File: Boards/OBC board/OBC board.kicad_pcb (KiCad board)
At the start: 4 copper layers, 75 x 48 mm, 92 parts, among them J1 BM03B-SRSS-TBLFSN, J2 USB_C, J3 Conn_01x01_Socket, J4 Conn_01x04_Socket, J5 Conn_01x04_Socket, J6 XT30UPB-M, J7 Conn_01x01_Socket, SW1 SW_Push, SW2 SW_Push, SW3 D2F-01-D, U1 ESD7L5.0DT5G, U10 IRLZ44NPBF, U2 ST1L05APU33R, U3 MAX485CSA+T, U4 ASM330LHH, U5 TPS1120DR, U6 TPS1120DR, U7 TPS1120DR, U8 LPS22DFTR, U9 LIS2MDLTR

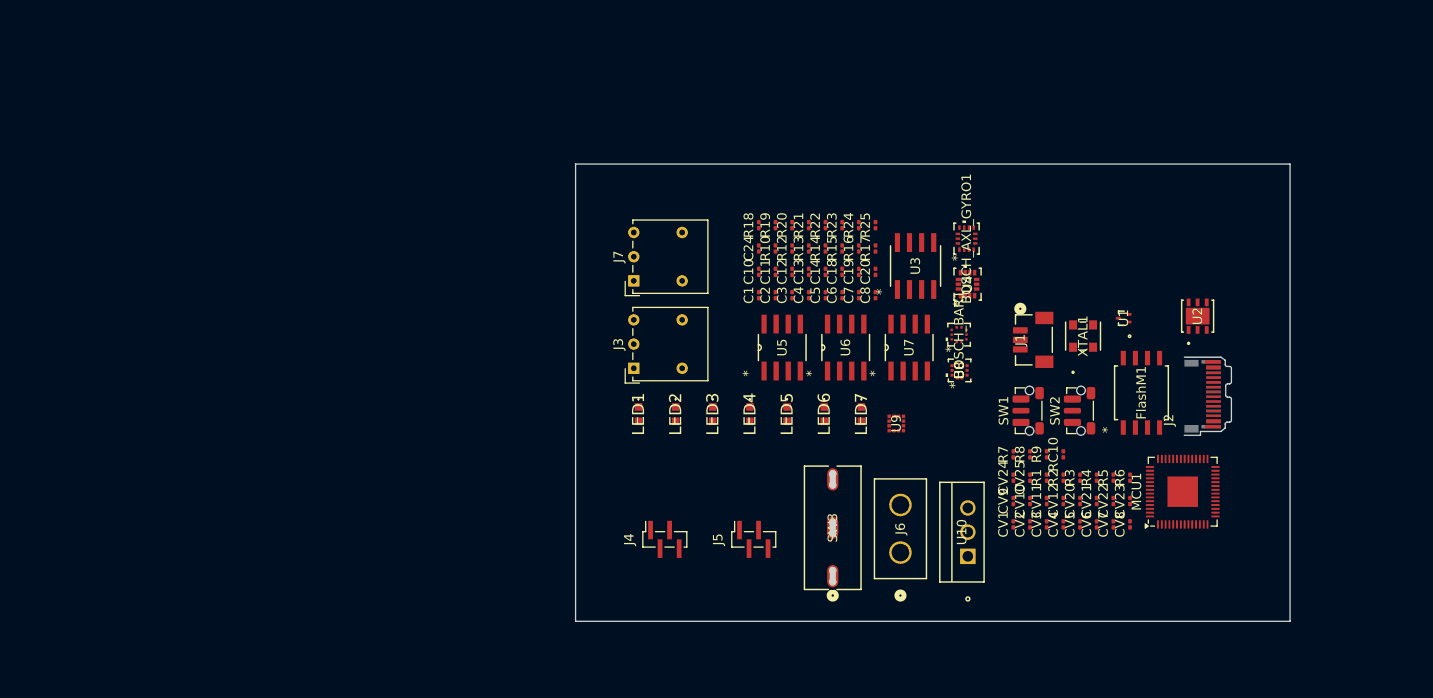
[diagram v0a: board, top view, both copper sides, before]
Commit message: Adição de Connectors
Connector "CONN Female Header 22022065" adicionado à library
Connectors do UART, 5V e GND adicionados à OBC
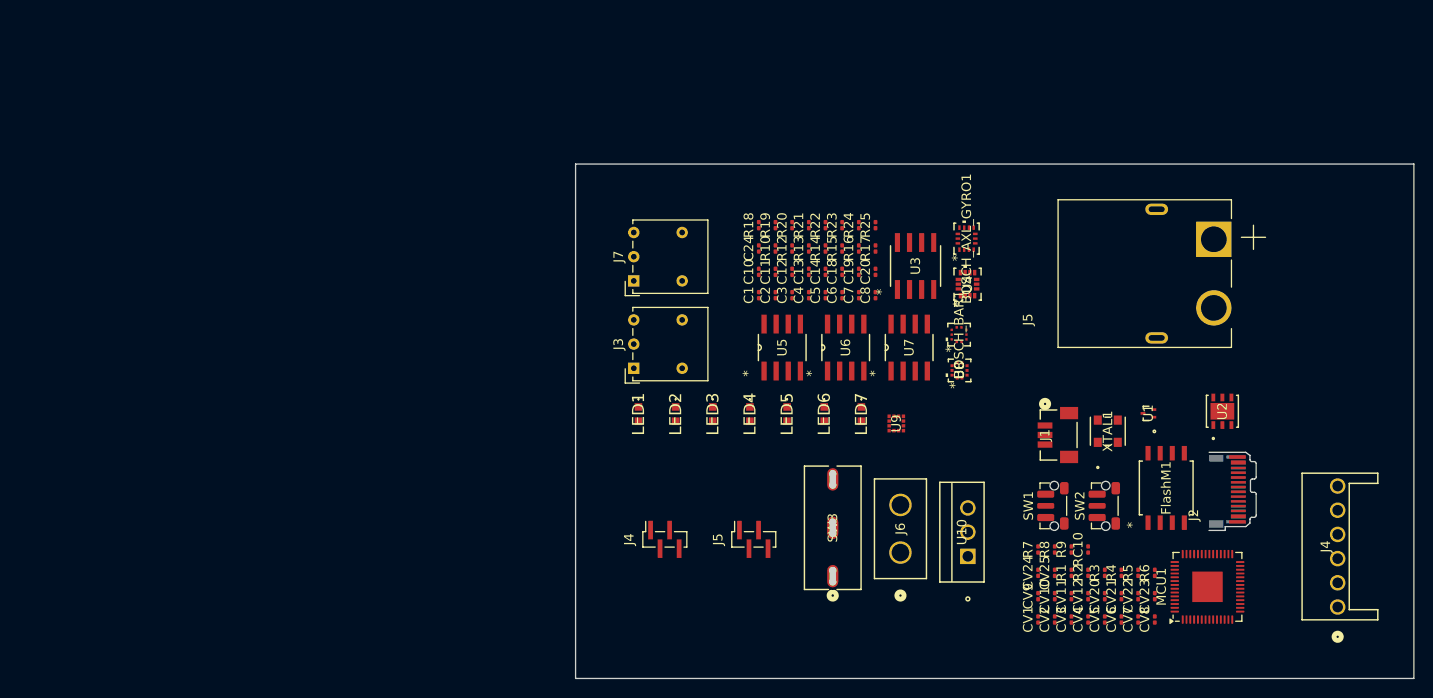
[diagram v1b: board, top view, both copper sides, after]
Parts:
- added J4: CONN_SA-4455_06_TE_MOL, CONN Female Header 22022065:CONN_SA-4455_06_TE_MOL, F.Cu at (160.5, 79.0)
- added J5: AMASS_XT60PW-M, Conn XT60PW-M:AMASS_XT60PW-M, F.Cu at (141.5, 44.0)
- R20, R21, R22, R23, R24, R25: value 30 -> 47
- moved R7 10.3 mm to (129.1, 73.0)
- moved J1 10.3 mm to (131.2, 60.9)
- moved J2 10.3 mm to (148.9, 66.7)
- moved R8 10.3 mm to (130.8, 73.0)
- moved R9 10.3 mm to (132.6, 73.0)
- moved RC10 10.3 mm to (134.3, 73.0)
- moved U1 10.3 mm to (140.6, 58.7)
- moved U2 10.3 mm to (148.4, 58.5)
- moved XTAL1 10.3 mm to (136.4, 60.5)
- moved CV1 10.3 mm to (129.1, 80.3)
- moved CV24 10.3 mm to (129.1, 75.4)
- moved CV9 10.3 mm to (129.1, 77.9)
- moved CV10 10.3 mm to (130.8, 77.9)
- moved CV11 10.3 mm to (132.6, 77.9)
- moved CV12 10.3 mm to (134.3, 77.9)
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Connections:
- R20 pad 1: Net-(LED2-A) -> Net-(U5-1SOURCE)
- R21 pad 1: Net-(LED3-A) -> Net-(U5-2SOURCE)
- R22 pad 1: Net-(LED4-A) -> Net-(U6-1SOURCE)
- R23 pad 1: Net-(LED5-A) -> Net-(U6-2SOURCE)
- R24 pad 1: Net-(LED6-A) -> Net-(U7-1SOURCE)
- R25 pad 1: Net-(LED7-A) -> Net-(U7-2SOURCE)
- U5 pad 1: Net-(LED2-K) -> Net-(U5-1SOURCE)
- U5 pad 3: Net-(LED3-K) -> Net-(U5-2SOURCE)
- U5 pad 5: GND -> Net-(LED3-A)
- U5 pad 6: GND -> Net-(LED3-A)
- U5 pad 7: GND -> Net-(LED2-A)
- U5 pad 8: GND -> Net-(LED2-A)
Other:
- board size 75 x 48 mm -> 88 x 54 mm

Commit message: Atualizações footprints
Adicionei a Resistência de 27 ohms que faltava na biblioteca Symbols Lib;
Atualizei as footprints do OBC menos a componente J6;
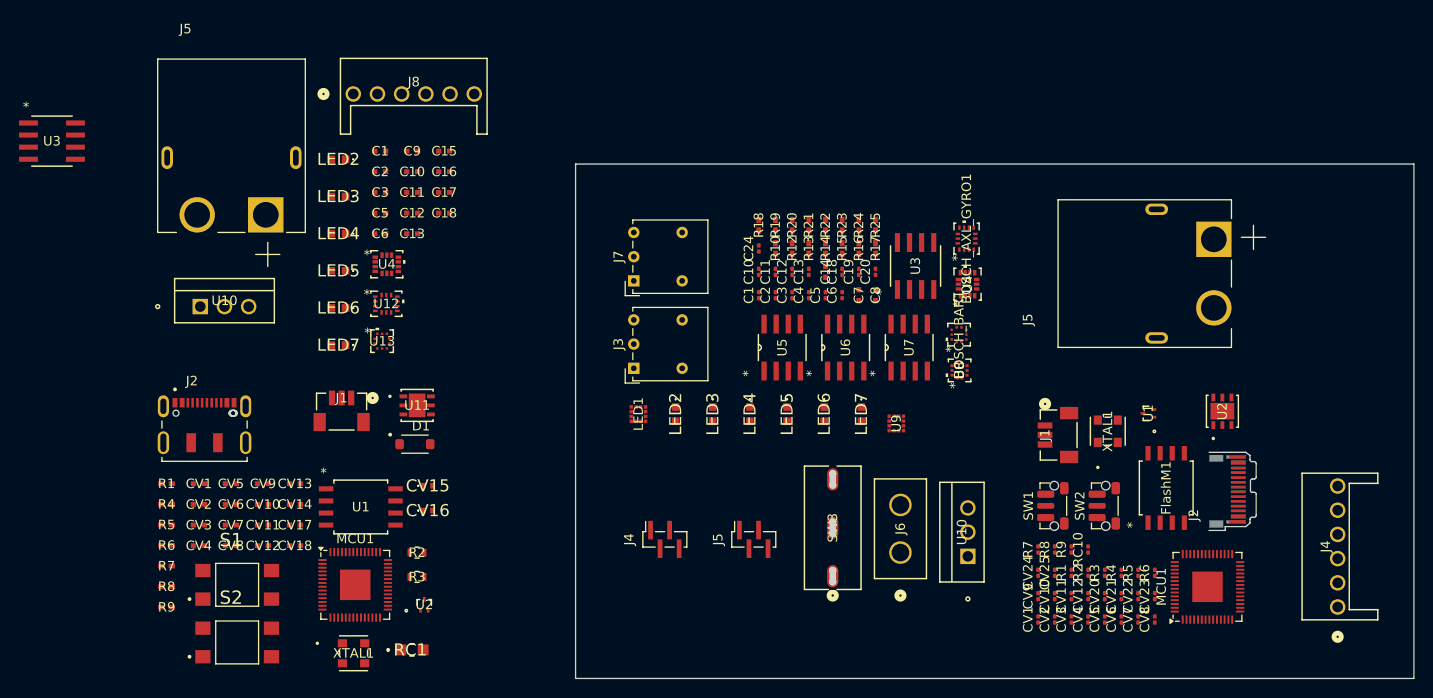
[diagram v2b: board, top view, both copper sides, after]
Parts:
- added C1: 100nF, CAP_GCM155_MUR:CAP_GCM155_MUR, F.Cu at (60.0, 31.1)
- added C10: 100nF, CAP_GCM155_MUR:CAP_GCM155_MUR, F.Cu at (63.3, 33.3)
- added C11: 100nF, CAP_GCM155_MUR:CAP_GCM155_MUR, F.Cu at (63.3, 35.5)
- added C12: 100nF, CAP_GCM155_MUR:CAP_GCM155_MUR, F.Cu at (63.3, 37.6)
- added C13: 100nF, CAP_GCM155_MUR:CAP_GCM155_MUR, F.Cu at (63.3, 39.8)
- added C15: 100nF, CAP_GCM155_MUR:CAP_GCM155_MUR, F.Cu at (66.7, 31.1)
- added C16: 100nF, CAP_GCM155_MUR:CAP_GCM155_MUR, F.Cu at (66.7, 33.3)
- added C17: 100nF, CAP_GCM155_MUR:CAP_GCM155_MUR, F.Cu at (66.7, 35.5)
- added C18: 10uF, CAP_GCM155_MUR:CAP_GCM155_MUR, F.Cu at (66.7, 37.6)
- added C2: 10nF, CAP_GCM155_MUR:CAP_GCM155_MUR, F.Cu at (60.0, 33.3)
- added C3: 10nF, CAP_GCM155_MUR:CAP_GCM155_MUR, F.Cu at (60.0, 35.5)
- added C5: 100nF, CAP_GCM155_MUR:CAP_GCM155_MUR, F.Cu at (60.0, 37.6)
- added C6: 100nF, CAP_GCM155_MUR:CAP_GCM155_MUR, F.Cu at (60.0, 39.8)
- added C9: 100nF, CAP_GCM155_MUR:CAP_GCM155_MUR, F.Cu at (63.3, 31.1)
- added CV1: 1uF, CAP_GCM155_MUR:CAP_GCM155_MUR, F.Cu at (41.0, 66.1)
- added CV10: 100nF, CAP_GCM155_MUR:CAP_GCM155_MUR, F.Cu at (47.7, 68.2)
- added CV11: 100nF, CAP_GCM155_MUR:CAP_GCM155_MUR, F.Cu at (47.7, 70.4)
- added CV12: 100nF, CAP_GCM155_MUR:CAP_GCM155_MUR, F.Cu at (47.7, 72.6)
- added CV13: 1uF, CAP_GCM155_MUR:CAP_GCM155_MUR, F.Cu at (51.0, 66.1)
- added CV14: 100nF, CAP_GCM155_MUR:CAP_GCM155_MUR, F.Cu at (51.0, 68.2)
- added CV15: 4.7uF, GRM15x:GRM15x, F.Cu at (65.0, 66.3)
- added CV16: 4.7uF, GRM15x:GRM15x, F.Cu at (65.0, 68.9)
- added CV17: 1uF, CAP_GCM155_MUR:CAP_GCM155_MUR, F.Cu at (51.0, 70.4)
- added CV18: 100nF, CAP_GCM155_MUR:CAP_GCM155_MUR, F.Cu at (51.0, 72.6)
- added CV2: 100nF, CAP_GCM155_MUR:CAP_GCM155_MUR, F.Cu at (41.0, 68.2)
- added CV3: 1uF, CAP_GCM155_MUR:CAP_GCM155_MUR, F.Cu at (41.0, 70.4)
- added CV4: 100nF, CAP_GCM155_MUR:CAP_GCM155_MUR, F.Cu at (41.0, 72.6)
- added CV5: 100nF, CAP_GCM155_MUR:CAP_GCM155_MUR, F.Cu at (44.3, 66.1)
- added CV6: 1uF, CAP_GCM155_MUR:CAP_GCM155_MUR, F.Cu at (44.3, 68.2)
- added CV7: 100nF, CAP_GCM155_MUR:CAP_GCM155_MUR, F.Cu at (44.3, 70.4)
- added CV8: 100nF, CAP_GCM155_MUR:CAP_GCM155_MUR, F.Cu at (44.3, 72.6)
- added CV9: 100nF, CAP_GCM155_MUR:CAP_GCM155_MUR, F.Cu at (47.7, 66.1)
- added D1: PMEG2010ER, PMEG2010ER:SODFL3517X110N, F.Cu at (63.6, 61.9)
- added J1: BM03B-SRSS-TBLFSN, SWD_Con:CONN_BM03B-SRSS-TBLFSN_JST, F.Cu at (55.9, 58.5)
- added J2: DX07S016JA1R1500, USBC-DX07S016JA1:JAE_DX07S016JA1R1500, F.Cu at (41.5, 58.7)
- added J5: XT60PW-M, Conn XT60PW-M:AMASS_XT60PW-M, F.Cu at (44.4, 31.8)
- added J8: 22022065, CONN Female Header:CONN_SA-4455_06_TE_MOL, F.Cu at (57.2, 25.1)
- added LED2: HSMH-H191, Red SMD LED:HSMHH191, F.Cu at (55.6, 32.0)
- added LED3: HSMH-H191, Red SMD LED:HSMHH191, F.Cu at (55.6, 35.9)
- added LED4: HSMH-H191, Red SMD LED:HSMHH191, F.Cu at (55.6, 39.8)
- added LED5: HSMH-H191, Red SMD LED:HSMHH191, F.Cu at (55.6, 43.7)
- added LED6: HSMH-H191, Red SMD LED:HSMHH191, F.Cu at (55.6, 47.6)
- added LED7: HSMH-H191, Red SMD LED:HSMHH191, F.Cu at (55.6, 51.5)
- added MCU1: RP2040, Package_DFN_QFN:QFN-56-1EP_7x7mm_P0.4mm_EP3.2x3.2mm, F.Cu at (57.4, 76.7)
- added R1: 1k, RC0402N_VIS:RC0402N_VIS, F.Cu at (37.6, 66.1)
- added R2: 27, KTR03EZPF27R0:RES_R0603_ROM, F.Cu at (63.9, 73.3)
- added R3: 27, KTR03EZPF27R0:RES_R0603_ROM, F.Cu at (63.9, 75.8)
- added R4: 100, RC0402N_VIS:RC0402N_VIS, F.Cu at (37.6, 68.2)
- added R5: 100, RC0402N_VIS:RC0402N_VIS, F.Cu at (37.6, 70.4)
- added R6: 1k, RC0402N_VIS:RC0402N_VIS, F.Cu at (37.6, 72.5)
- added R7: 10k, RC0402N_VIS:RC0402N_VIS, F.Cu at (37.6, 74.7)
- added R8: 1k, RC0402N_VIS:RC0402N_VIS, F.Cu at (37.6, 76.9)
- added R9: 5k1, RC0402N_VIS:RC0402N_VIS, F.Cu at (37.6, 79.0)
- added RC1: 5k1, ERA6AEB101V:ERA6AEB101V, F.Cu at (63.3, 83.5)
- added S1: TL3305CF160QG, E-Switch_7mm:SW_TL3305CF160QG, F.Cu at (45.0, 76.7)
- added S2: TL3305CF160QG, E-Switch_7mm:SW_TL3305CF160QG, F.Cu at (45.0, 82.7)
- added U1: W25Q128JVSIQ TR, NOR Flash:SOIC_208MIL_WIN, F.Cu at (58.0, 68.5)
- added U10: IRLZ44NPBF, NMOS IRLZ44:PG-TO220-3_INF, F.Cu at (41.1, 47.5)
- added U11: ST1L05APU33R, LDO ST1L05A:DFN_5APU33R_STM, F.Cu at (63.9, 57.8)
- added U12: BMI323, IMU BMI323:BMI323_BOS, F.Cu at (60.6, 47.2)
- added U13: BMP581, BARO BMP581:QFN10_BMP581_BOS, F.Cu at (60.2, 51.1)
- added U2: ESD7L5.0DT5G, ESD7L5-Diode:SOT-723_0P85X1P25_ONS, F.Cu at (64.6, 78.8)
- added U3: MAX485CSA+T, RS Transceiver:21-0041-3-M_90-0096-8L_MXM, F.Cu at (25.5, 30.1)
- added U4: ASM330LHHTR, IMU ASM330LHHTR:LGA-14L_2P5X3X0P83_STM, F.Cu at (60.7, 43.0)
- added XTAL1: ASE-12.000MHZ-LC-T, AS12MHz:ASE-3.2X2.5_ABR, F.Cu at (57.2, 83.9)
- C14, C7, C8: footprint Capacitor_SMD:C_0201_0603Metric -> CAP_GCM155_MUR:CAP_GCM155_MUR
- LED1: footprint Red SMD LED:HSMHH191 -> MAG LIS2MDLTR:LGA-12_2X2X1_STM
- R10, R12, R13, R14, R15, R16, R17, R18, R19, R20, R21, R22, R23, R24, R25: footprint Resistor_SMD:R_0201_0603Metric -> RC0402N_VIS:RC0402N_VIS
- U5, U6, U7: footprint Dual PMOS:D8 -> 2 PMOS:D8
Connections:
- R12 pad 2: +5V -> /+5V
- R14 pad 1: +5V -> /+5V
- U6 pad 1: Net-(LED4-K) -> Net-(U6-1SOURCE)
- U6 pad 3: Net-(LED5-K) -> Net-(U6-2SOURCE)
- U6 pad 5: GND -> Net-(LED5-A)
- U6 pad 6: GND -> Net-(LED5-A)
- U6 pad 7: GND -> Net-(LED4-A)
- U6 pad 8: GND -> Net-(LED4-A)
- U7 pad 1: Net-(LED6-K) -> Net-(U7-1SOURCE)
- U7 pad 3: Net-(LED7-K) -> Net-(U7-2SOURCE)
- U7 pad 5: GND -> Net-(LED7-A)
- U7 pad 6: GND -> Net-(LED7-A)
- U7 pad 7: GND -> Net-(LED6-A)
- U7 pad 8: GND -> Net-(LED6-A)
- U8 pad 2: /SPI0_SCK -> (no net)

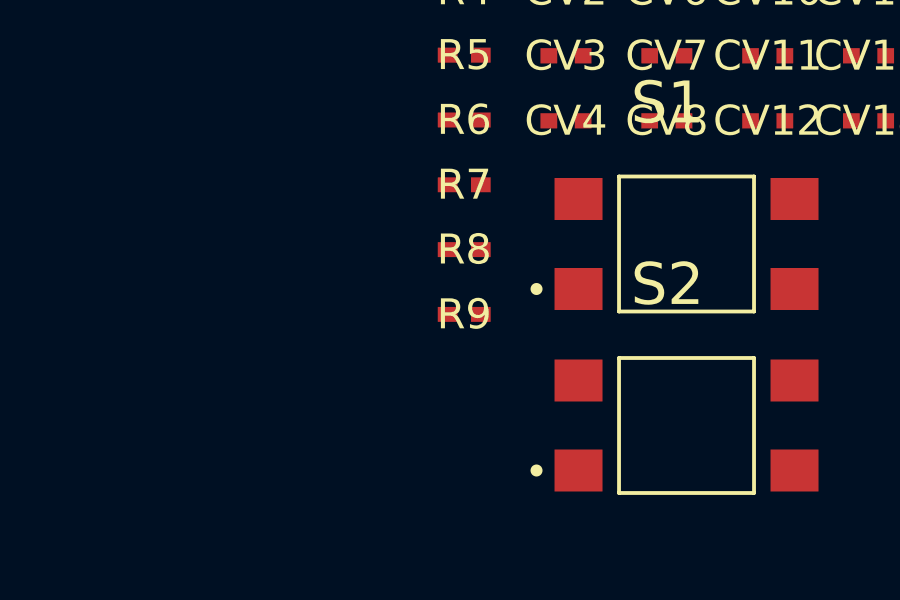
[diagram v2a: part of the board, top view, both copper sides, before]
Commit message: Mudança de nome das footprints
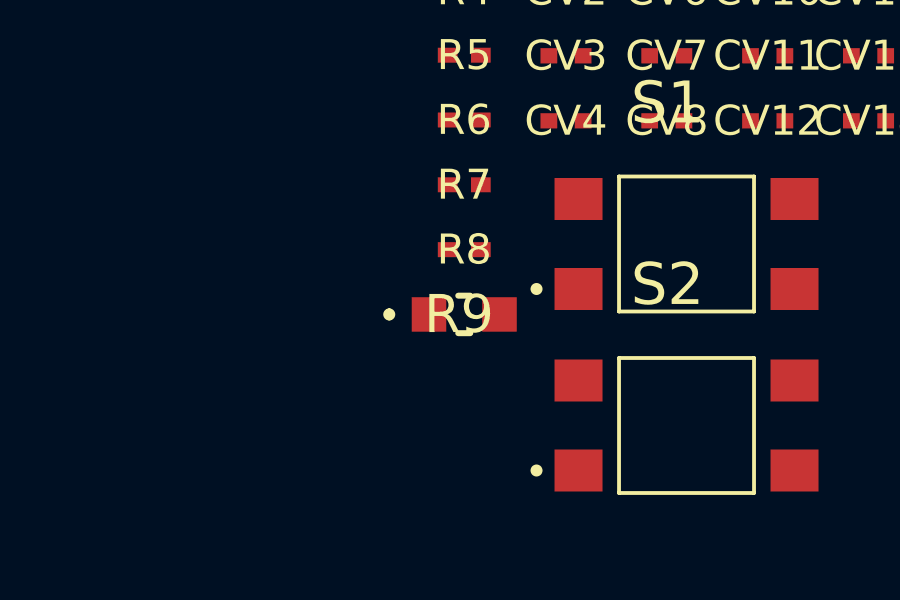
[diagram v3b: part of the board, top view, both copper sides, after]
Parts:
- C1, C10, C11, C12, C13, C14, C15, C16, C17, C18, C2, C3, C5, C6, C7, C8, C9, CV1, CV10, CV11, CV12, CV13, CV14, CV17, CV18, CV2, CV3, CV4, CV5, CV6, CV7, CV8, CV9: footprint CAP_GCM155_MUR:CAP_GCM155_MUR -> Capacitor_0402:Capacitor_0402
- CV15, CV16: footprint GRM15x:GRM15x -> C_4uF7_0402:C_4uF7_0402
- R1, R10, R12, R13, R14, R15, R16, R17, R18, R19, R20, R21, R22, R23, R24, R25, R4, R5, R6, R7, R8: footprint RC0402N_VIS:RC0402N_VIS -> RES_0402:RES_0402
- R2, R3: footprint KTR03EZPF27R0:RES_R0603_ROM -> RES_R0603_27:RES_R0603_27
- R9: footprint RC0402N_VIS:RC0402N_VIS -> R_0805_5K1:R_0805_5K1
- RC1: footprint ERA6AEB101V:ERA6AEB101V -> R_0805_5K1:R_0805_5K1
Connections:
- J6 pad 1: Net-(U10-D) -> Net-(J6-Pad1)
